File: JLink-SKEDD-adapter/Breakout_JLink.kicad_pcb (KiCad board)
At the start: 2 copper layers, 27.4 x 26 mm, 5 parts, among them J1 UART_ClientSide, J2 Conn_02x10_Odd_Even, J3 Jitter_Debug_HostSide, J4 Conn_01x06_Female

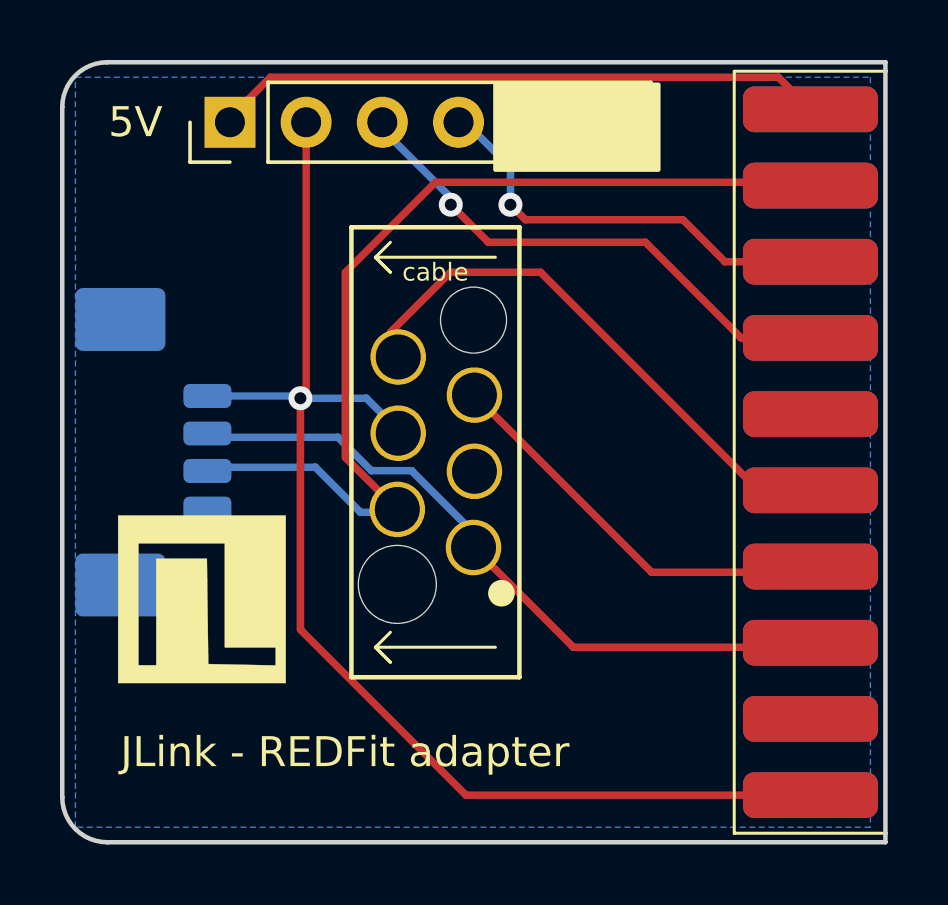
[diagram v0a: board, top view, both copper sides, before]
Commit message: Breakout JLink: rotate SKEDD footprint with correct cable orientation
(the previous version works OK but the silkscreen arrows point the wrong way)
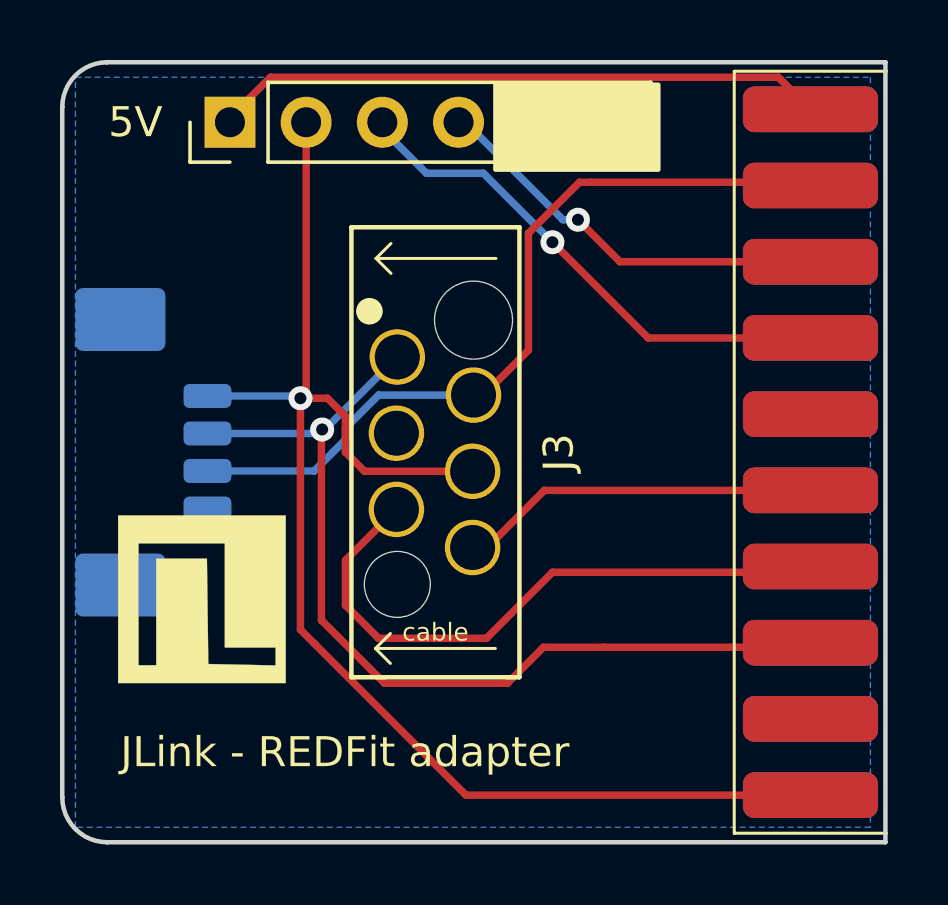
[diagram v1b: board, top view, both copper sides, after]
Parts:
- J3: footprint Jitter_FootPrints:WR-WST_REDFIT-6-pins_490107670612 -> Jitter_Footprints:WR-WST_REDFIT-6-pins_490107670612-adapter_to_pcb
- turned J3 to 90 degrees
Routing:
- net /Tx_JLink: track 24.2 -> 31.9 mm, vias 0 -> 1
- net /SWDIO: track 13.6 -> 20.8 mm
- net /SWDCLK: track 18.8 -> 12.0 mm
- net /Rx_JLink: track 32.6 -> 26.6 mm
- net VCC: track 43.5 -> 46.9 mm
- net /nRESET: track 14.2 -> 13.4 mm

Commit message: Breakout JLink: release V2
- inline UART tx resistor to handle conflict if JLink + Blackmagic hosts both connected
- UART rx pullup resistor to avoid noise if target disconnected or in reset
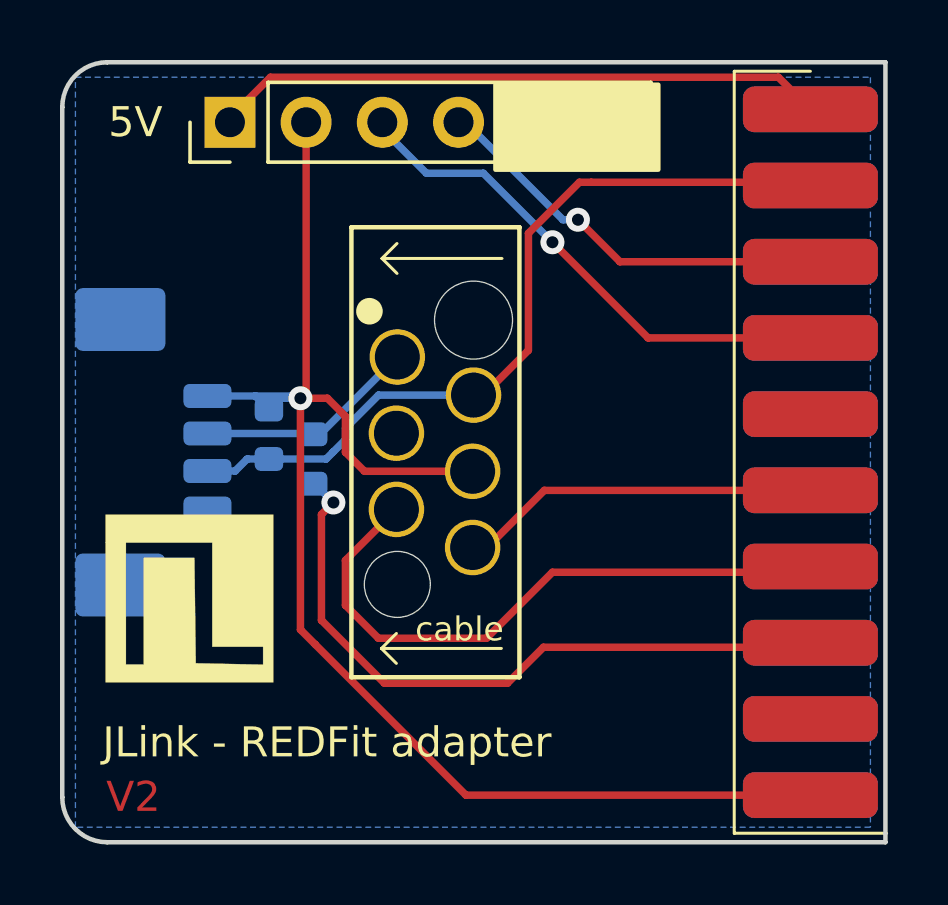
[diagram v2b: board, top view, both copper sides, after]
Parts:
- added R1: 100, Resistor_SMD:R_0603_1608Metric, B.Cu at (183.4, 85.2)
- added R2: 10k, Resistor_SMD:R_0603_1608Metric, B.Cu at (181.9, 84.4)
- moved LOGO1 0.42 mm to (178.8, 90.0)
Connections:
- J1 pad 3: /Tx_JLink -> Net-(J1-RX_(client))
- J3 pad 1: /Tx_JLink -> Net-(J1-RX_(client))
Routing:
- net /Tx_JLink: track 31.9 -> 23.2 mm
- net Net-(J1-RX_(client)): track 0.00 -> 7.39 mm
- net VCC: track 46.9 -> 48.7 mm
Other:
- board text added: "V2"
